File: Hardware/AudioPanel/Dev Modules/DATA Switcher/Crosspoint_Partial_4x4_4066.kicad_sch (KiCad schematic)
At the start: 26 parts, among them U901 74HC4066BQ, U902 74HC4066BQ, U903 74HC4066BQ

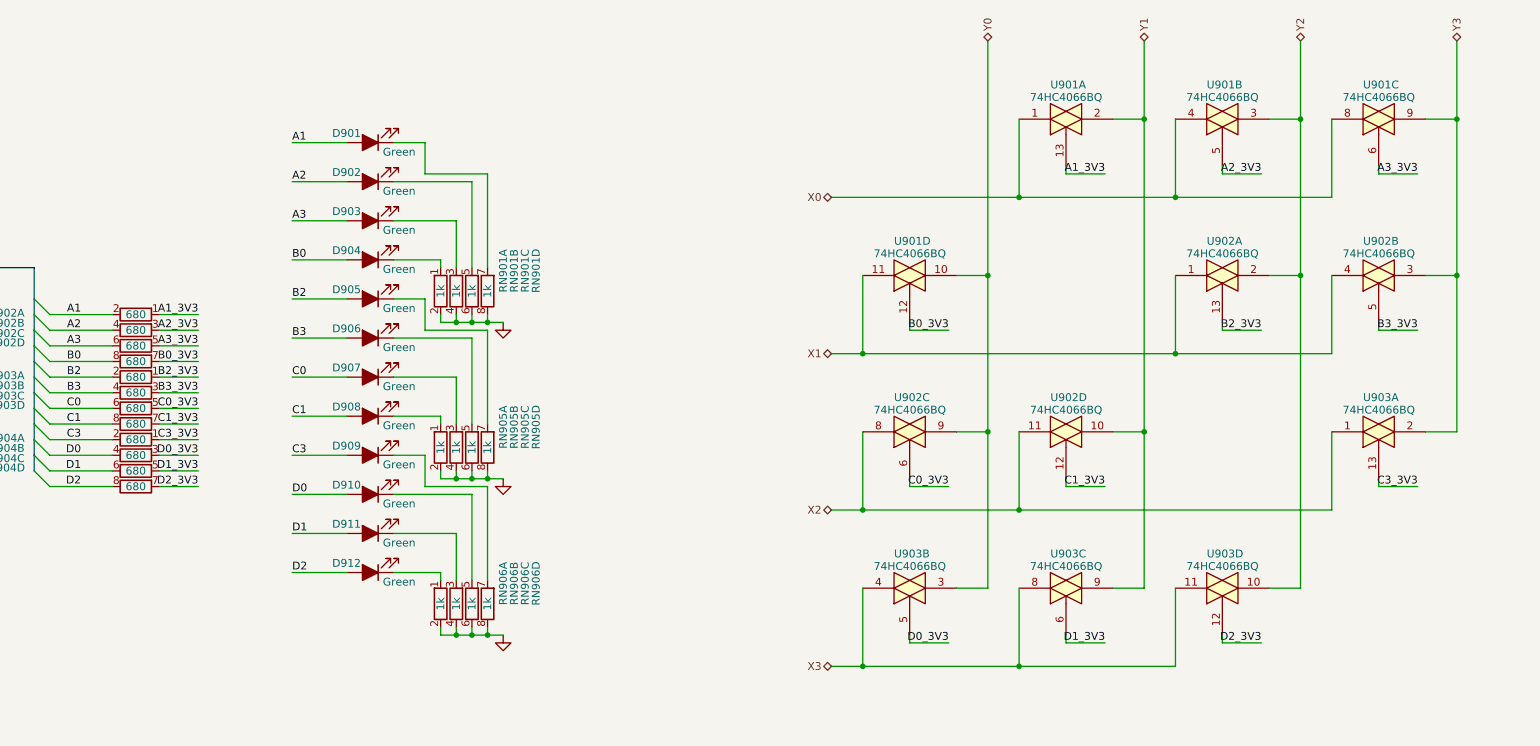
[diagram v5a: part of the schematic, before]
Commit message: Fixed footprint errors, placed onto PCBs
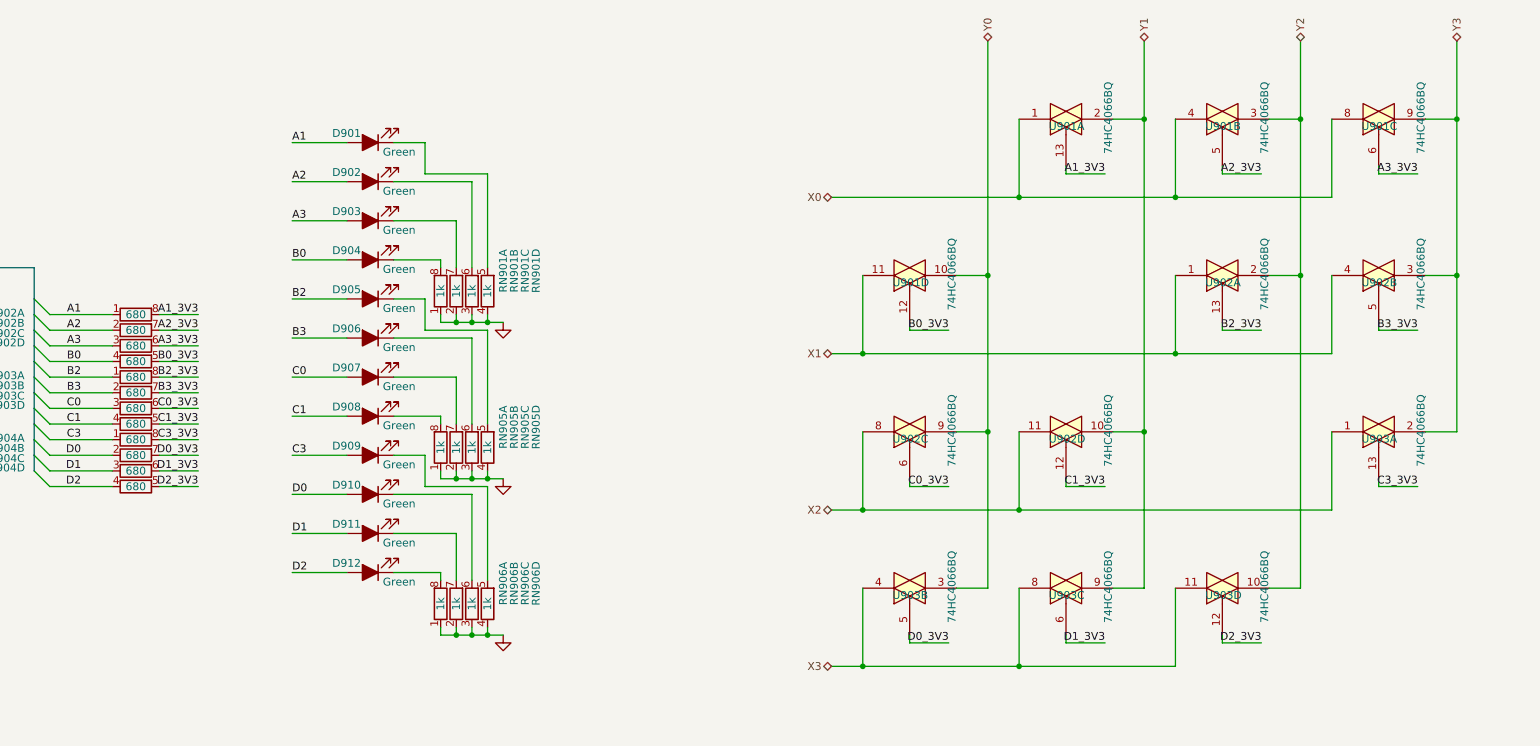
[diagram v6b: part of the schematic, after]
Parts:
- RN901, RN902, RN903, RN904, RN905, RN906: symbol Library_MicSwitcher:R_Network04_Split -> Libraries:R_Network04_Split
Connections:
- net A1: now also RN902.1 (4); no longer RN902.2
- net A1_3V3: now also RN902.8; no longer RN902.1
- net A2: now also RN902.2; no longer RN902.4
- net A2_3V3: now also RN902.7 (5); no longer RN902.3
- net A3: now also RN902.3; no longer RN902.6
- net A3_3V3: now also RN902.6; no longer RN902.5
- net B0: now also RN902.4; no longer RN902.8
- net B0_3V3: now also RN902.5; no longer RN902.7
- net B2: now also RN903.1 (4); no longer RN903.2
- net B2_3V3: now also RN903.8; no longer RN903.1
- net B3: now also RN903.2; no longer RN903.4
- net B3_3V3: now also RN903.7 (5); no longer RN903.3
- net C0: now also RN903.3; no longer RN903.6
- net C0_3V3: now also RN903.6; no longer RN903.5
- net C1: now also RN903.4; no longer RN903.8
- net C1_3V3: now also RN903.5; no longer RN903.7
- net C3: now also RN904.1 (4); no longer RN904.2
- net C3_3V3: now also RN904.8; no longer RN904.1
- net D0: now also RN904.2; no longer RN904.4
- net D0_3V3: now also RN904.7 (5); no longer RN904.3
- net D1: now also RN904.3; no longer RN904.6
- net D1_3V3: now also RN904.6; no longer RN904.5
- net D2: now also RN904.4; no longer RN904.8
- net D2_3V3: now also RN904.5; no longer RN904.7
- net GND: now also RN901.1 (4), RN901.2, RN901.3, RN901.4, RN905.1 (4), RN905.2, RN905.3, RN905.4, RN906.1 (4), RN906.2, RN906.3, RN906.4; no longer RN901.2, RN901.4, RN901.6, RN901.8, RN905.2, RN905.4, RN905.6, RN905.8, RN906.2, RN906.4, RN906.6, RN906.8
- net VDD: now also U901.15 (VDD), U902.15 (VDD), U903.15 (VDD)
- net at D908.1 (K): now also RN905.8; no longer RN905.1
- net at D910.1 (K): now also RN906.6; no longer RN906.5
- net at D902.1 (K): now also RN901.6; no longer RN901.5
- net at D901.1 (K): now also RN901.5; no longer RN901.7
- net at D909.1 (K): now also RN906.5; no longer RN906.7
- net at D905.1 (K): now also RN905.5; no longer RN905.7
- net at D904.1 (K): now also RN901.8; no longer RN901.1
- net at D906.1 (K): now also RN905.6; no longer RN905.5
- net at D903.1 (K): now also RN901.7 (5); no longer RN901.3
- net at D911.1 (K): now also RN906.7 (5); no longer RN906.3
- net at D907.1 (K): now also RN905.7 (5); no longer RN905.3
- net at D912.1 (K): now also RN906.8; no longer RN906.1

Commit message: Changed LED and Resistor Array packages
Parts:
- D901, D902, D903, D904, D905, D906, D907, D908, D909, D910, D911, D912: footprint LED_SMD:LED_0603_1608Metric -> Libraries:Worthington_LED_0603
- RN901, RN902, RN903, RN904, RN905, RN906: footprint Resistor_SMD:R_Array_Convex_4x1206 -> Libraries:RES_ARRAY_4RES_0804
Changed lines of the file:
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@@
 			)
 		)
-		(property "Footprint" "LED_SMD:LED_0603_1608Metric"
+		(property "Footprint" "Libraries:Worthington_LED_0603"
 			(at 96.52 105.41 0)
 			(effects
@@
 			)
 		)
-		(property "Footprint" "Resistor_SMD:R_Array_Convex_4x1206"
+		(property "Footprint" "Libraries:RES_ARRAY_4RES_0804"
 			(at 58.42 113.792 90)
 			(effects
@@
 			)
 		)
-		(property "Footprint" "Resistor_SMD:R_Array_Convex_4x1206"
+		(property "Footprint" "Libraries:RES_ARRAY_4RES_0804"
 			(at 110.998 135.89 90)
 			(effects
@@
 			)
 		)
-		(property "Footprint" "Resistor_SMD:R_Array_Convex_4x1206"
+		(property "Footprint" "Libraries:RES_ARRAY_4RES_0804"
 			(at 58.42 98.552 90)
 			(effects
@@
 			)
 		)
-		(property "Footprint" "LED_SMD:LED_0603_1608Metric"
+		(property "Footprint" "Libraries:Worthington_LED_0603"
 			(at 96.52 67.31 0)
 			(effects
@@
 			)
 		)
-		(property "Footprint" "Resistor_SMD:R_Array_Convex_4x1206"
+		(property "Footprint" "Libraries:RES_ARRAY_4RES_0804"
 			(at 113.538 85.09 90)
 			(effects
@@
 			)
 		)
-		(property "Footprint" "LED_SMD:LED_0603_1608Metric"
+		(property "Footprint" "Libraries:Worthington_LED_0603"
 			(at 96.52 111.76 0)
 			(effects
@@
 			)
 		)
-		(property "Footprint" "LED_SMD:LED_0603_1608Metric"
+		(property "Footprint" "Libraries:Worthington_LED_0603"
 			(at 96.52 60.96 0)
 			(effects
@@
 			)
 		)
-		(property "Footprint" "Resistor_SMD:R_Array_Convex_4x1206"
+		(property "Footprint" "Libraries:RES_ARRAY_4RES_0804"
 			(at 113.538 135.89 90)
 			(effects
@@
 			)
 		)
-		(property "Footprint" "Resistor_SMD:R_Array_Convex_4x1206"
+		(property "Footprint" "Libraries:RES_ARRAY_4RES_0804"
 			(at 110.998 85.09 90)
 			(effects
@@
 			)
 		)
-		(property "Footprint" "Resistor_SMD:R_Array_Convex_4x1206"
+		(property "Footprint" "Libraries:RES_ARRAY_4RES_0804"
 			(at 113.538 110.49 90)
 			(effects
@@
 			)
 		)
-		(property "Footprint" "Resistor_SMD:R_Array_Convex_4x1206"
+		(property "Footprint" "Libraries:RES_ARRAY_4RES_0804"
 			(at 109.982 85.09 90)
 			(effects
@@
 			)
 		)
-		(property "Footprint" "Resistor_SMD:R_Array_Convex_4x1206"
+		(property "Footprint" "Libraries:RES_ARRAY_4RES_0804"
 			(at 110.998 110.49 90)
 			(effects
@@
 			)
 		)
-		(property "Footprint" "Resistor_SMD:R_Array_Convex_4x1206"
+		(property "Footprint" "Libraries:RES_ARRAY_4RES_0804"
 			(at 58.42 101.092 90)
 			(effects
@@
 			)
 		)
-		(property "Footprint" "Resistor_SMD:R_Array_Convex_4x1206"
+		(property "Footprint" "Libraries:RES_ARRAY_4RES_0804"
 			(at 108.458 85.09 90)
 			(effects
@@
 			)
 		)
-		(property "Footprint" "LED_SMD:LED_0603_1608Metric"
+		(property "Footprint" "Libraries:Worthington_LED_0603"
 			(at 96.52 92.71 0)
 			(effects
@@
 			)
 		)
-		(property "Footprint" "Resistor_SMD:R_Array_Convex_4x1206"
+		(property "Footprint" "Libraries:RES_ARRAY_4RES_0804"
 			(at 58.42 106.172 90)
 			(effects
@@
 			)
 		)
-		(property "Footprint" "LED_SMD:LED_0603_1608Metric"
+		(property "Footprint" "Libraries:Worthington_LED_0603"
 			(at 96.52 124.46 0)
 			(effects
@@
 			)
 		)
-		(property "Footprint" "Resistor_SMD:R_Array_Convex_4x1206"
+		(property "Footprint" "Libraries:RES_ARRAY_4RES_0804"
 			(at 108.458 135.89 90)
 			(effects
@@
 			)
 		)
-		(property "Footprint" "LED_SMD:LED_0603_1608Metric"
+		(property "Footprint" "Libraries:Worthington_LED_0603"
 			(at 96.52 80.01 0)
 			(effects
@@
 			)
 		)
-		(property "Footprint" "Resistor_SMD:R_Array_Convex_4x1206"
+		(property "Footprint" "Libraries:RES_ARRAY_4RES_0804"
 			(at 58.42 118.872 90)
 			(effects
@@
 			)
 		)
-		(property "Footprint" "LED_SMD:LED_0603_1608Metric"
+		(property "Footprint" "Libraries:Worthington_LED_0603"
 			(at 96.52 73.66 0)
 			(effects
@@
 			)
 		)
-		(property "Footprint" "LED_SMD:LED_0603_1608Metric"
+		(property "Footprint" "Libraries:Worthington_LED_0603"
 			(at 96.52 86.36 0)
 			(effects
@@
 			)
 		)
-		(property "Footprint" "Resistor_SMD:R_Array_Convex_4x1206"
+		(property "Footprint" "Libraries:RES_ARRAY_4RES_0804"
 			(at 58.42 108.712 90)
 			(effects
@@
 			)
 		)
-		(property "Footprint" "Resistor_SMD:R_Array_Convex_4x1206"
+		(property "Footprint" "Libraries:RES_ARRAY_4RES_0804"
 			(at 109.982 110.49 90)
 			(effects
@@
 			)
 		)
-		(property "Footprint" "LED_SMD:LED_0603_1608Metric"
+		(property "Footprint" "Libraries:Worthington_LED_0603"
 			(at 96.52 99.06 0)
 			(effects
@@
 			)
 		)
-		(property "Footprint" "Resistor_SMD:R_Array_Convex_4x1206"
+		(property "Footprint" "Libraries:RES_ARRAY_4RES_0804"
 			(at 58.42 96.012 90)
 			(effects
@@
 			)
 		)
-		(property "Footprint" "Resistor_SMD:R_Array_Convex_4x1206"
+		(property "Footprint" "Libraries:RES_ARRAY_4RES_0804"
 			(at 109.982 135.89 90)
 			(effects
@@
 			)
 		)
-		(property "Footprint" "Resistor_SMD:R_Array_Convex_4x1206"
+		(property "Footprint" "Libraries:RES_ARRAY_4RES_0804"
 			(at 58.42 93.472 90)
 			(effects
@@
 			)
 		)
-		(property "Footprint" "LED_SMD:LED_0603_1608Metric"
+		(property "Footprint" "Libraries:Worthington_LED_0603"
 			(at 96.52 118.11 0)
 			(effects
@@
 			)
 		)
-		(property "Footprint" "Resistor_SMD:R_Array_Convex_4x1206"
+		(property "Footprint" "Libraries:RES_ARRAY_4RES_0804"
 			(at 58.42 116.332 90)
 			(effects
@@
 			)
 		)
-		(property "Footprint" "Resistor_SMD:R_Array_Convex_4x1206"
+		(property "Footprint" "Libraries:RES_ARRAY_4RES_0804"
 			(at 58.42 103.632 90)
 			(effects
@@
 			)
 		)
-		(property "Footprint" "Resistor_SMD:R_Array_Convex_4x1206"
+		(property "Footprint" "Libraries:RES_ARRAY_4RES_0804"
 			(at 108.458 110.49 90)
 			(effects
@@
 			)
 		)
-		(property "Footprint" "Resistor_SMD:R_Array_Convex_4x1206"
+		(property "Footprint" "Libraries:RES_ARRAY_4RES_0804"
 			(at 58.42 111.252 90)
 			(effects
@@
 			)
 		)
-		(property "Footprint" "Resistor_SMD:R_Array_Convex_4x1206"
+		(property "Footprint" "Libraries:RES_ARRAY_4RES_0804"
 			(at 58.42 90.932 90)
 			(effects
@@
 			)
 		)
-		(property "Footprint" "LED_SMD:LED_0603_1608Metric"
+		(property "Footprint" "Libraries:Worthington_LED_0603"
 			(at 96.52 130.81 0)
 			(effects

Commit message: Routing progress
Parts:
- added C906: 22uF, Libraries:Worthington_C_0603, symbol Device:C_Small
- U901, U902, U903: symbol 4xxx:4066 -> Libraries:74HC4066BQ
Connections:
- net A1: now also RN904.4; no longer RN902.1 (4)
- net A2: now also RN902.1 (4); no longer RN902.2
- net A3: now also RN904.3; no longer RN902.3
- net B0: now also RN903.1 (4); no longer RN902.4
- net B2: now also RN902.2; no longer RN903.1 (4)
- net B3: now also RN902.3; no longer RN903.2
- net C0: now also RN904.1 (4); no longer RN903.3
- net C1: now also RN904.2; no longer RN903.4
- net C3: now also RN902.4; no longer RN904.1 (4)
- net D0: now also RN903.2; no longer RN904.2
- net D1: now also RN903.4; no longer RN904.3
- net D2: now also RN903.3; no longer RN904.4
- net GND: now also C906.2
- net VDD: now also C906.1
- net X0: now also U901.11, U901.2, U901.3; no longer U901.1, U901.4, U901.8
- net X1: now also U901.8, U902.3, U903.3; no longer U901.11, U902.1, U902.4
- net X2: now also U902.10, U902.2, U902.9; no longer U902.11, U902.8, U903.1
- net X3: now also U903.10, U903.2, U903.9; no longer U903.11, U903.4, U903.8
- net Y0: now also U902.11, U903.4, U903.8; no longer U901.10, U902.9, U903.3
- net Y1: now also U901.1, U902.1, U903.1; no longer U901.2, U902.10, U903.9
- net Y2: now also U901.4, U901.9, U903.11; no longer U901.3, U902.2, U903.10
- net Y3: now also U901.10, U902.4, U902.8; no longer U901.9, U902.3, U903.2
- net at RN901.5: now also D903.1 (K); no longer D901.1 (K)
- net at RN905.5: now also D906.1 (K); no longer D905.1 (K)
- net at RN905.6: now also D905.1 (K); no longer D906.1 (K)
- net at RN901.7 (5): now also D901.1 (K); no longer D903.1 (K)
- net A1_3V3 renamed A1_T
- net A1_T: now also RN904.5; no longer RN902.8
- net A2_3V3 renamed A2_T
- net A2_T: now also RN902.8; no longer RN902.7 (5)
- net A3_3V3 renamed B2_T
- net B2_T: now also RN902.7 (5); no longer RN902.6
- net B0_3V3 renamed A3_T
- net A3_T: now also RN904.6; no longer RN902.5
- net B2_3V3 renamed B0_T
- net B0_T: now also U903.5; no longer U902.13
- net B3_3V3 renamed B3_T
- net B3_T: now also RN902.6; no longer RN903.7 (5)
- net C0_3V3 renamed C3_T
- net C3_T: now also RN902.5; no longer RN903.6
- net C1_3V3 renamed C0_T
- net C0_T: now also RN904.8; no longer RN903.5
- net C3_3V3 renamed D1_T
- net D1_T: now also RN903.5; no longer RN904.8
- net D0_3V3 renamed C1_T
- net C1_T: now also U902.13; no longer U903.5
- net D1_3V3 renamed D0_T
- net D0_T: now also RN903.7 (5); no longer RN904.6
- net D2_3V3 renamed D2_T
- net D2_T: now also RN903.6; no longer RN904.5
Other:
- moved on the sheet: RN901B, RN901D, RN902A, RN902B, RN902C, RN902D, RN903A, RN903B, RN903C, RN903D, RN904A, RN904B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
